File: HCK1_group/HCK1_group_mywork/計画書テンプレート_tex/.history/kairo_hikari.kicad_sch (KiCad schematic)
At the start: 2 parts, among them J1 Conn_01x04

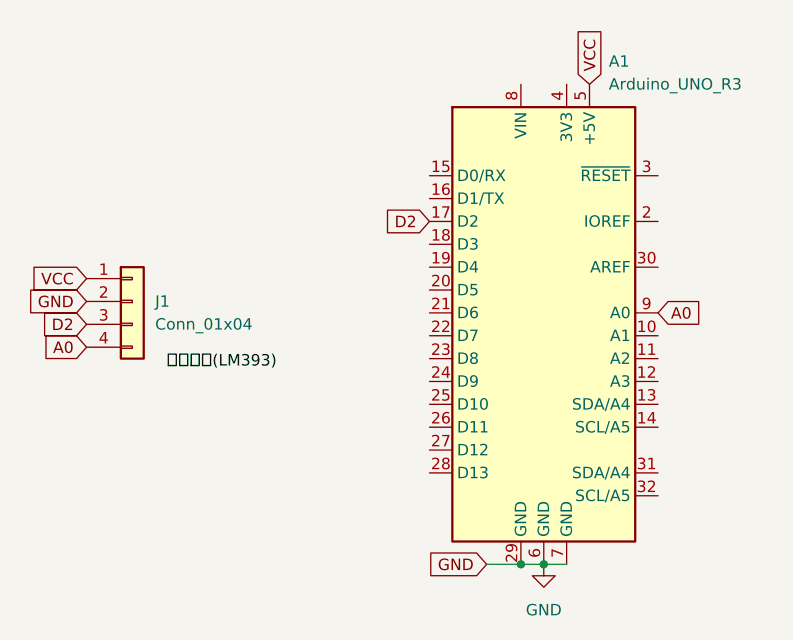
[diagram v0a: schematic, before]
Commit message: これまでの作業を反映: コード・計画書・回路図・作業ログ等を更新
- 指揮デバイス(shiki_device.ino): 音量用可変抵抗器をA5に変更、段階表示デバッグを改善
- 表示デバイス(Display.ino)、可変抵抗器検証(slider_test)を更新・追加
- 最終計画書・再計画書・設計関連ドキュメント、KiCad回路図を更新
- 第六/七回作業ログを整理、不要ファイル・旧資料を削除
- 設計用画像・図表を追加

注: ネストしたgitリポジトリ HCK1_group/yama は除外（別途submodule化が必要）

Co-Authored-By: Claude Opus 4.8 <noreply@anthropic.com>
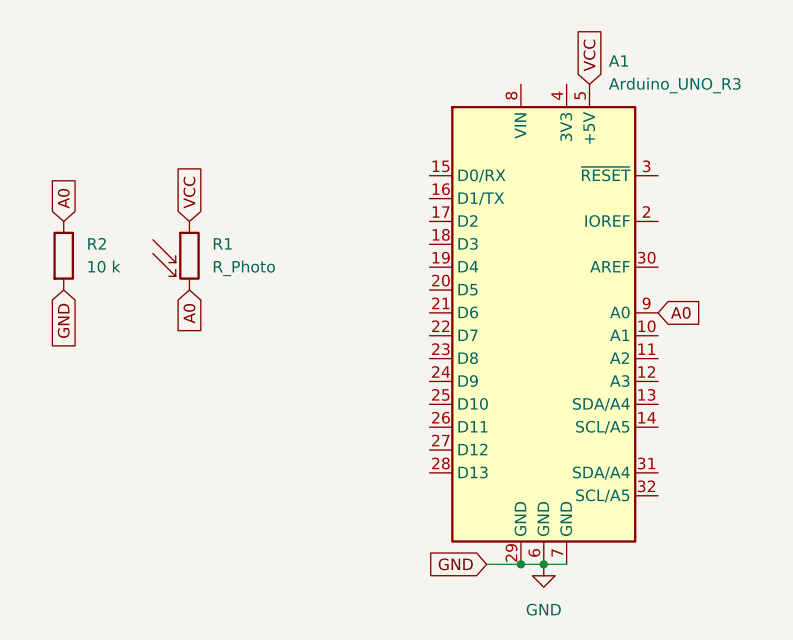
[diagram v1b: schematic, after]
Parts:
- removed J1: Conn_01x04, symbol Connector_Generic:Conn_01x04
- added R1: R_Photo, symbol Device:R_Photo
- added R2: 10 k, symbol Device:R
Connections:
- net A0: now also R1.2, R2.1
- net GND: now also R2.2
- net VCC: now also R1.1
- net D2: no longer names the net of A1.17 (D2)
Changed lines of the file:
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@@
 		)
 	)
-	(label "光センサ(LM393)"
-		(at 139.7 92.71 0)
-		(effects
-			(font
-				(size 1.27 1.27)
-			)
-			(justify left bottom)
+	(global_label "VCC"
+		(shape input)
+		(at 142.24 76.2 90)
+		(fields_autoplaced yes)
+		(effects
+			(font
+				(size 1.27 1.27)
+			)
+			(justify left)
+		)
+		(property "Intersheetrefs" "${INTERSHEET_REFS}"
+			(at 142.24 69.5862 90)
+			(hide yes)
+			(show_name no)
+			(do_not_autoplace no)
+			(effects
+				(font
+					(size 1.27 1.27)
+				)
+				(justify left)
+			)
 		)
 	)
@@
 	(global_label "GND"
 		(shape input)
-		(at 130.81 85.09 180)
+		(at 175.26 114.3 180)
 		(fields_autoplaced yes)
 		(effects
@@
 		)
 		(property "Intersheetrefs" "${INTERSHEET_REFS}"
-			(at 123.9543 85.09 0)
+			(at 168.4043 114.3 0)
 			(hide yes)
 			(show_name no)
@@
 		)
 	)
+	(global_label "A0"
+		(shape input)
+		(at 142.24 83.82 270)
+		(fields_autoplaced yes)
+		(effects
+			(font
+				(size 1.27 1.27)
+			)
+			(justify right)
+		)
+		(property "Intersheetrefs" "${INTERSHEET_REFS}"
+			(at 142.24 89.1033 90)
+			(hide yes)
+			(show_name no)
+			(do_not_autoplace no)
+			(effects
+				(font
+					(size 1.27 1.27)
+				)
+				(justify right)
+			)
+		)
+	)
+	(global_label "A0"
+		(shape input)
+		(at 128.27 76.2 90)
+		(fields_autoplaced yes)
+		(effects
+			(font
+				(size 1.27 1.27)
+			)
+			(justify left)
+		)
+		(property "Intersheetrefs" "${INTERSHEET_REFS}"
+			(at 128.27 70.9167 90)
+			(hide yes)
+			(show_name no)
+			(do_not_autoplace no)
+			(effects
+				(font
+					(size 1.27 1.27)
+				)
+				(justify left)
+			)
+		)
+	)
 	(global_label "GND"
 		(shape input)
-		(at 175.26 114.3 180)
+		(at 128.27 83.82 270)
 		(fields_autoplaced yes)
 		(effects
@@
 		)
 		(property "Intersheetrefs" "${INTERSHEET_REFS}"
-			(at 168.4043 114.3 0)
+			(at 128.27 90.6757 90)
 			(hide yes)
 			(show_name no)
@@
 		)
 	)
-	(global_label "A0"
-		(shape input)
-		(at 130.81 90.17 180)
-		(fields_autoplaced yes)
-		(effects
-			(font
-				(size 1.27 1.27)
-			)
-			(justify right)
-		)
-		(property "Intersheetrefs" "${INTERSHEET_REFS}"
-			(at 125.5267 90.17 0)
-			(hide yes)
-			(show_name no)
-			(do_not_autoplace no)
-			(effects
-				(font
-					(size 1.27 1.27)
-				)
-				(justify right)
-			)
-		)
-	)
-	(global_label "D2"
-		(shape input)
-		(at 168.91 76.2 180)
-		(fields_autoplaced yes)
-		(effects
-			(font
-				(size 1.27 1.27)
-			)
-			(justify right)
-		)
-		(property "Intersheetrefs" "${INTERSHEET_REFS}"
-			(at 163.4453 76.2 0)
-			(hide yes)
-			(show_name no)
-			(do_not_autoplace no)
-			(effects
-				(font
-					(size 1.27 1.27)
-				)
-				(justify right)
-			)
-		)
-	)
-	(global_label "D2"
-		(shape input)
-		(at 130.81 87.63 180)
-		(fields_autoplaced yes)
-		(effects
-			(font
-				(size 1.27 1.27)
-			)
-			(justify right)
-		)
-		(property "Intersheetrefs" "${INTERSHEET_REFS}"
-			(at 125.3453 87.63 0)
-			(hide yes)
-			(show_name no)
-			(do_not_autoplace no)
-			(effects
-				(font
-					(size 1.27 1.27)
-				)
-				(justify right)
-			)
-		)
-	)
 	(global_label "VCC"
 		(shape input)
-		(at 130.81 82.55 180)
-		(fields_autoplaced yes)
-		(effects
-			(font
-				(size 1.27 1.27)
-			)
-			(justify right)
-		)
-		(property "Intersheetrefs" "${INTERSHEET_REFS}"
-			(at 124.1962 82.55 0)
-			(hide yes)
-			(show_name no)
-			(do_not_autoplace no)
-			(effects
-				(font
-					(size 1.27 1.27)
-				)
-				(justify right)
-			)
-		)
-	)
-	(global_label "VCC"
-		(shape input)
 		(at 186.69 60.96 90)
 		(fields_autoplaced yes)
@@
 				)
 				(justify left)
-			)
-		)
-	)
-	(symbol
-		(lib_id "Connector_Generic:Conn_01x04")
-		(at 135.89 85.09 0)
-		(unit 1)
-		(body_style 1)
-		(exclude_from_sim no)
-		(in_bom yes)
-		(on_board yes)
-		(in_pos_files yes)
-		(dnp no)
-		(fields_autoplaced yes)
-		(property "Reference" "J1"
-			(at 138.43 85.0899 0)
-			(show_name no)
-			(do_not_autoplace no)
-			(effects
-				(font
-					(size 1.27 1.27)
-				)
-				(justify left)
-			)
-		)
-		(property "Value" "Conn_01x04"
-			(at 138.43 87.6299 0)
-			(show_name no)
-			(do_not_autoplace no)
-			(effects
-				(font
-					(size 1.27 1.27)
-				)
-				(justify left)
-			)
-		)
-		(property "Footprint" ""
-			(at 135.89 85.09 0)
-			(hide yes)
-			(show_name no)
-			(do_not_autoplace no)
-			(effects
-				(font
-					(size 1.27 1.27)
-				)
-			)
-		)
-		(property "Datasheet" ""
-			(at 135.89 85.09 0)
-			(hide yes)
-			(show_name no)
-			(do_not_autoplace no)
-			(effects
-				(font
-					(size 1.27 1.27)
-				)
-			)
-		)
-		(property "Description" "Generic connector, single row, 01x04, script generated (kicad-library-utils/schlib/autogen/connector/)"
-			(at 135.89 85.09 0)
-			(hide yes)
-			(show_name no)
-			(do_not_autoplace no)
-			(effects
-				(font
-					(size 1.27 1.27)
-				)
-			)
-		)
-		(pin "1"
-		)
-		(pin "4"
-		)
-		(pin "2"
-		)
-		(pin "3"
-		)
-		(instances
-			(project "kairo_hikari"
-				(path "/1f92bd14-ea7d-4dc8-b986-7a3530d2e4e6"
-					(reference "J1")
-					(unit 1)
-				)
 			)
 		)
@@
 					(unit 1)
 				)
+			)
+		)
+	)
+	(symbol
+		(lib_id "Device:R")
+		(at 128.27 80.01 0)
+		(unit 1)
+		(body_style 1)
+		(exclude_from_sim no)
+		(in_bom yes)
+		(on_board yes)
+		(in_pos_files yes)
+		(dnp no)
+		(fields_autoplaced yes)
+		(property "Reference" "R2"
+			(at 130.81 78.7399 0)
+			(show_name no)
+			(do_not_autoplace no)
+			(effects
+				(font
+					(size 1.27 1.27)
+				)
+				(justify left)
+			)
+		)
+		(property "Value" "10 k"
+			(at 130.81 81.2799 0)
+			(show_name no)
+			(do_not_autoplace no)
+			(effects
+				(font
+					(size 1.27 1.27)
+				)
+				(justify left)
+			)
+		)
+		(property "Footprint" ""
+			(at 126.492 80.01 90)
+			(hide yes)
+			(show_name no)
+			(do_not_autoplace no)
+			(effects
+				(font
+					(size 1.27 1.27)
+				)
+			)
+		)
+		(property "Datasheet" ""
+			(at 128.27 80.01 0)
+			(hide yes)
+			(show_name no)
+			(do_not_autoplace no)
+			(effects
+				(font
+					(size 1.27 1.27)
+				)
+			)
+		)
+		(property "Description" "Resistor"
+			(at 128.27 80.01 0)
+			(hide yes)
+			(show_name no)
+			(do_not_autoplace no)
+			(effects
+				(font
+					(size 1.27 1.27)
+				)
+			)
+		)
+		(pin "1"
+		)
+		(pin "2"
+		)
+		(instances
+			(project "kairo_hikari"
+				(path "/1f92bd14-ea7d-4dc8-b986-7a3530d2e4e6"
+					(reference "R2")
+					(unit 1)
+				)
+			)
+		)
+	)
+	(symbol
+		(lib_id "Device:R_Photo")
+		(at 142.24 80.01 0)
+		(unit 1)
+		(body_style 1)
+		(exclude_from_sim no)
+		(in_bom yes)
+		(on_board yes)
+		(in_pos_files yes)
+		(dnp no)
+		(fields_autoplaced yes)
+		(property "Reference" "R1"
+			(at 144.78 78.7399 0)
+			(show_name no)
+			(do_not_autoplace no)
+			(effects
+				(font
+					(size 1.27 1.27)
+				)
+				(justify left)
+			)
+		)
+		(property "Value" "R_Photo"
+			(at 144.78 81.2799 0)
+			(show_name no)
+			(do_not_autoplace no)
+			(effects
+				(font
+					(size 1.27 1.27)
+				)
+				(justify left)
+			)
+		)
+		(property "Footprint" ""
+			(at 143.51 86.36 90)
+			(hide yes)
+			(show_name no)
+			(do_not_autoplace no)
+			(effects
+				(font
+					(size 1.27 1.27)
+				)
+				(justify left)
+			)
+		)
+		(property "Datasheet" ""
+			(at 142.24 81.28 0)
+			(hide yes)
+			(show_name no)
+			(do_not_autoplace no)
+			(effects
+				(font
+					(size 1.27 1.27)
+				)
+			)
+		)
+		(property "Description" "Photoresistor"
+			(at 142.24 80.01 0)
+			(hide yes)
+			(show_name no)
+			(do_not_autoplace no)
+			(effects
+				(font
+					(size 1.27 1.27)
+				)
+			)
+		)
+		(pin "1"
+		)
+		(pin "2"
+		)
+		(instances
+			(project "kairo_hikari"
+				(path "/1f92bd14-ea7d-4dc8-b986-7a3530d2e4e6"
+					(reference "R1")
+					(unit 1)
+				)
